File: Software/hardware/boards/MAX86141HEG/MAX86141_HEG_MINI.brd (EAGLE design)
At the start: 65 x 9.9 mm, 18 parts, among them U1 MAX86141ENP+T, U3 TXBN0304RUTR, U4 LP5907MFX-3.3/NOPB

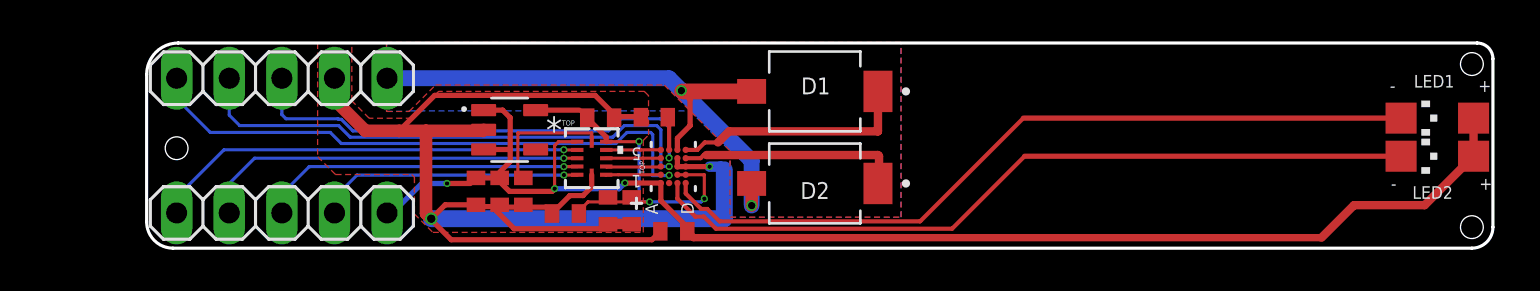
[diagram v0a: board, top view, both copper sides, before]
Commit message: lolin32 firmware should update properly now
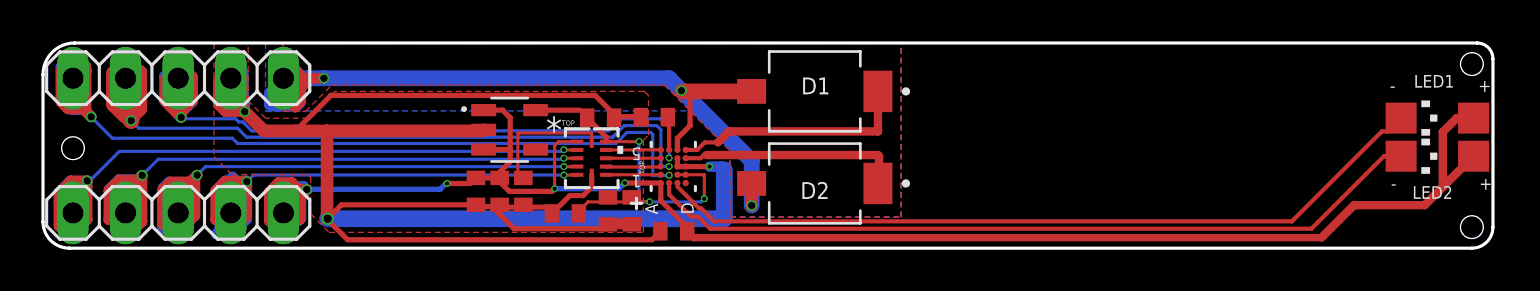
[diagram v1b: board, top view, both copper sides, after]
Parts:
- moved JP2 5.00 mm to (127.8, 20.1)
- moved JP3 5.00 mm to (127.8, 13.6)
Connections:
- removed net LED1: LED1.C, U1.D1
- new net LED3: LED2.C, U1.B1
- net LED2: now also LED1.C; no longer LED2.C
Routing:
- net LED1: track 38.0 -> 0.00 mm
- net LED3: track 0.00 -> 37.9 mm
- net GND: track 74.5 -> 108.5 mm, vias 2 -> 3
- net 3.3V: track 68.0 -> 91.1 mm, vias 3 -> 4
- net INT: track 27.9 -> 50.0 mm, vias 1 -> 2
- net SDO3.3: track 15.9 -> 37.4 mm, vias 1 -> 2
- net CSB3.3: track 21.2 -> 40.9 mm, vias 1 -> 2
- net SCLK3.3: track 12.8 -> 31.3 mm, vias 1 -> 2
- net SDI3.3: track 18.9 -> 36.7 mm, vias 1 -> 2
- net GPIO2: track 22.7 -> 39.8 mm, vias 1 -> 2
- net GPIO1: track 25.5 -> 42.5 mm, vias 1 -> 2
- net PD_GND: track 29.1 -> 42.8 mm, vias 2 -> 3
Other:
- board size 65 x 9.9 mm -> 70 x 9.9 mm
